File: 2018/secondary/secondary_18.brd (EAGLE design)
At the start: 160 x 173.7 mm, 35 parts, among them Q1 BUZ11BV, Q2 BUZ11BV

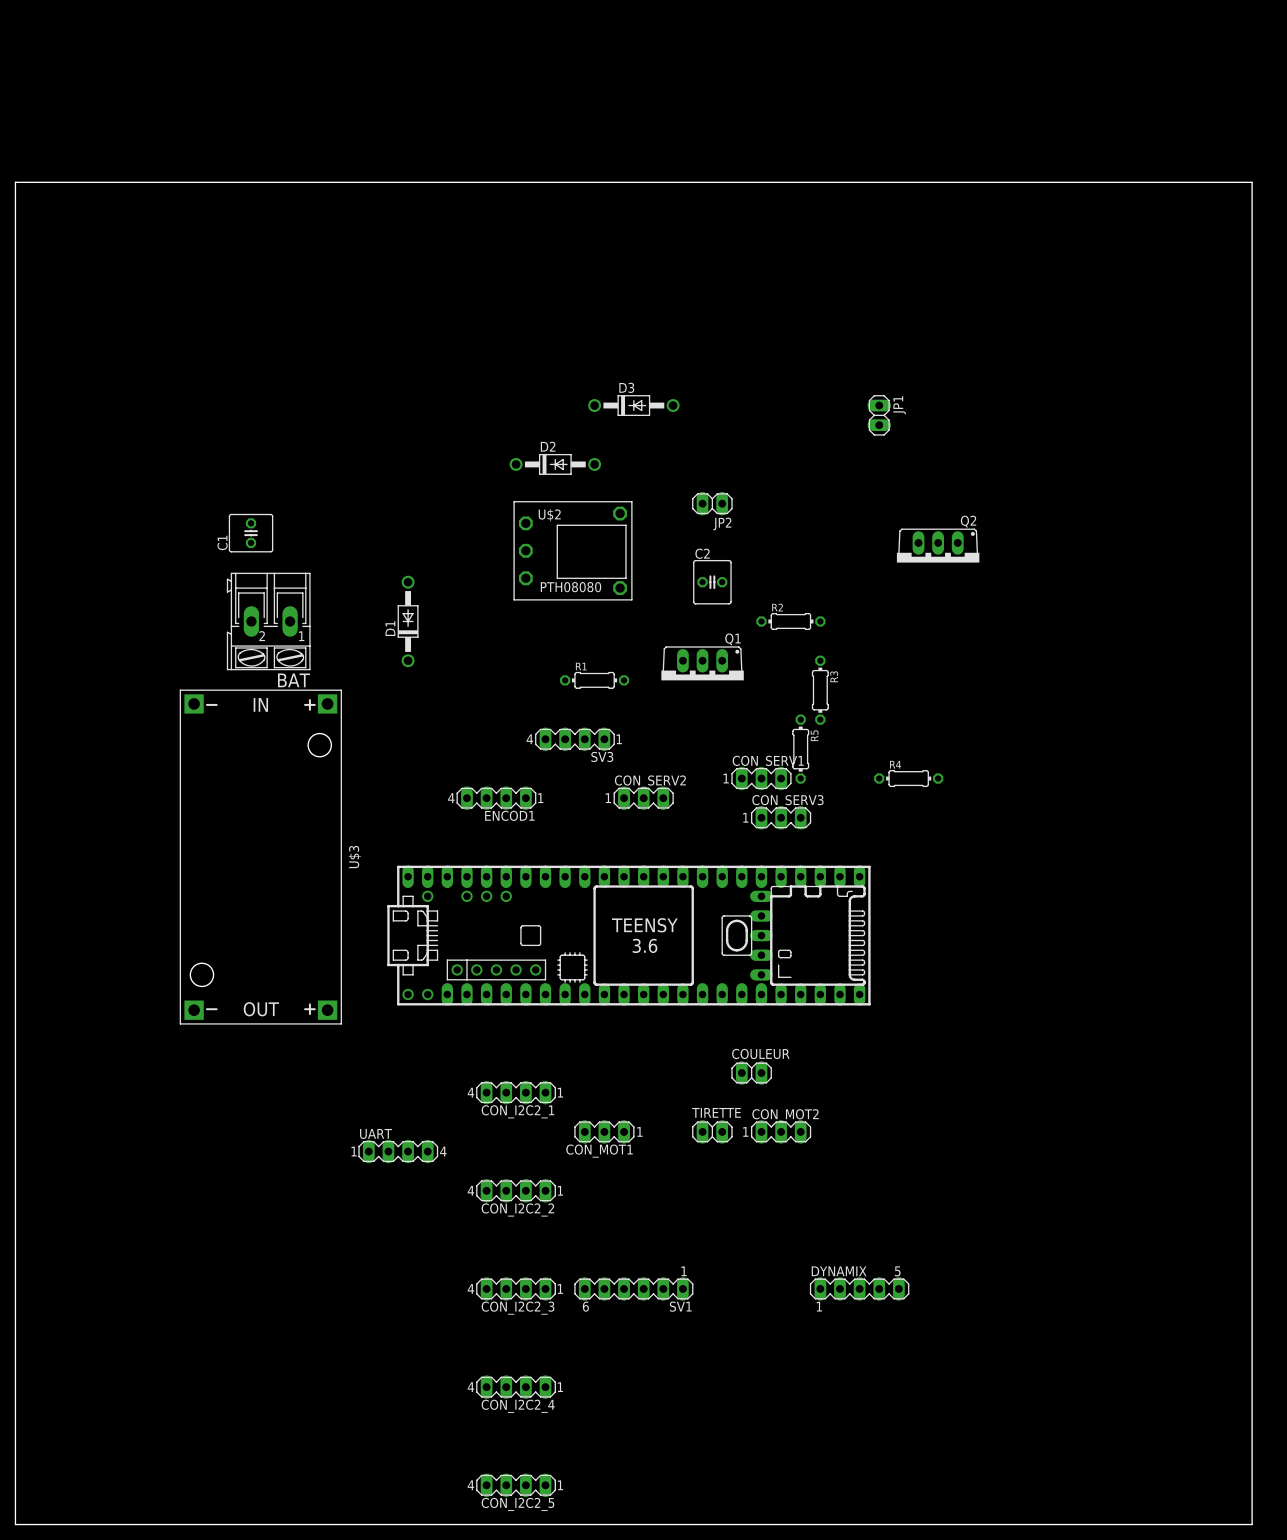
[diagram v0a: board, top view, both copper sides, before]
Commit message: [secondary 2018] Modificates the position of the elements above the x abscisse
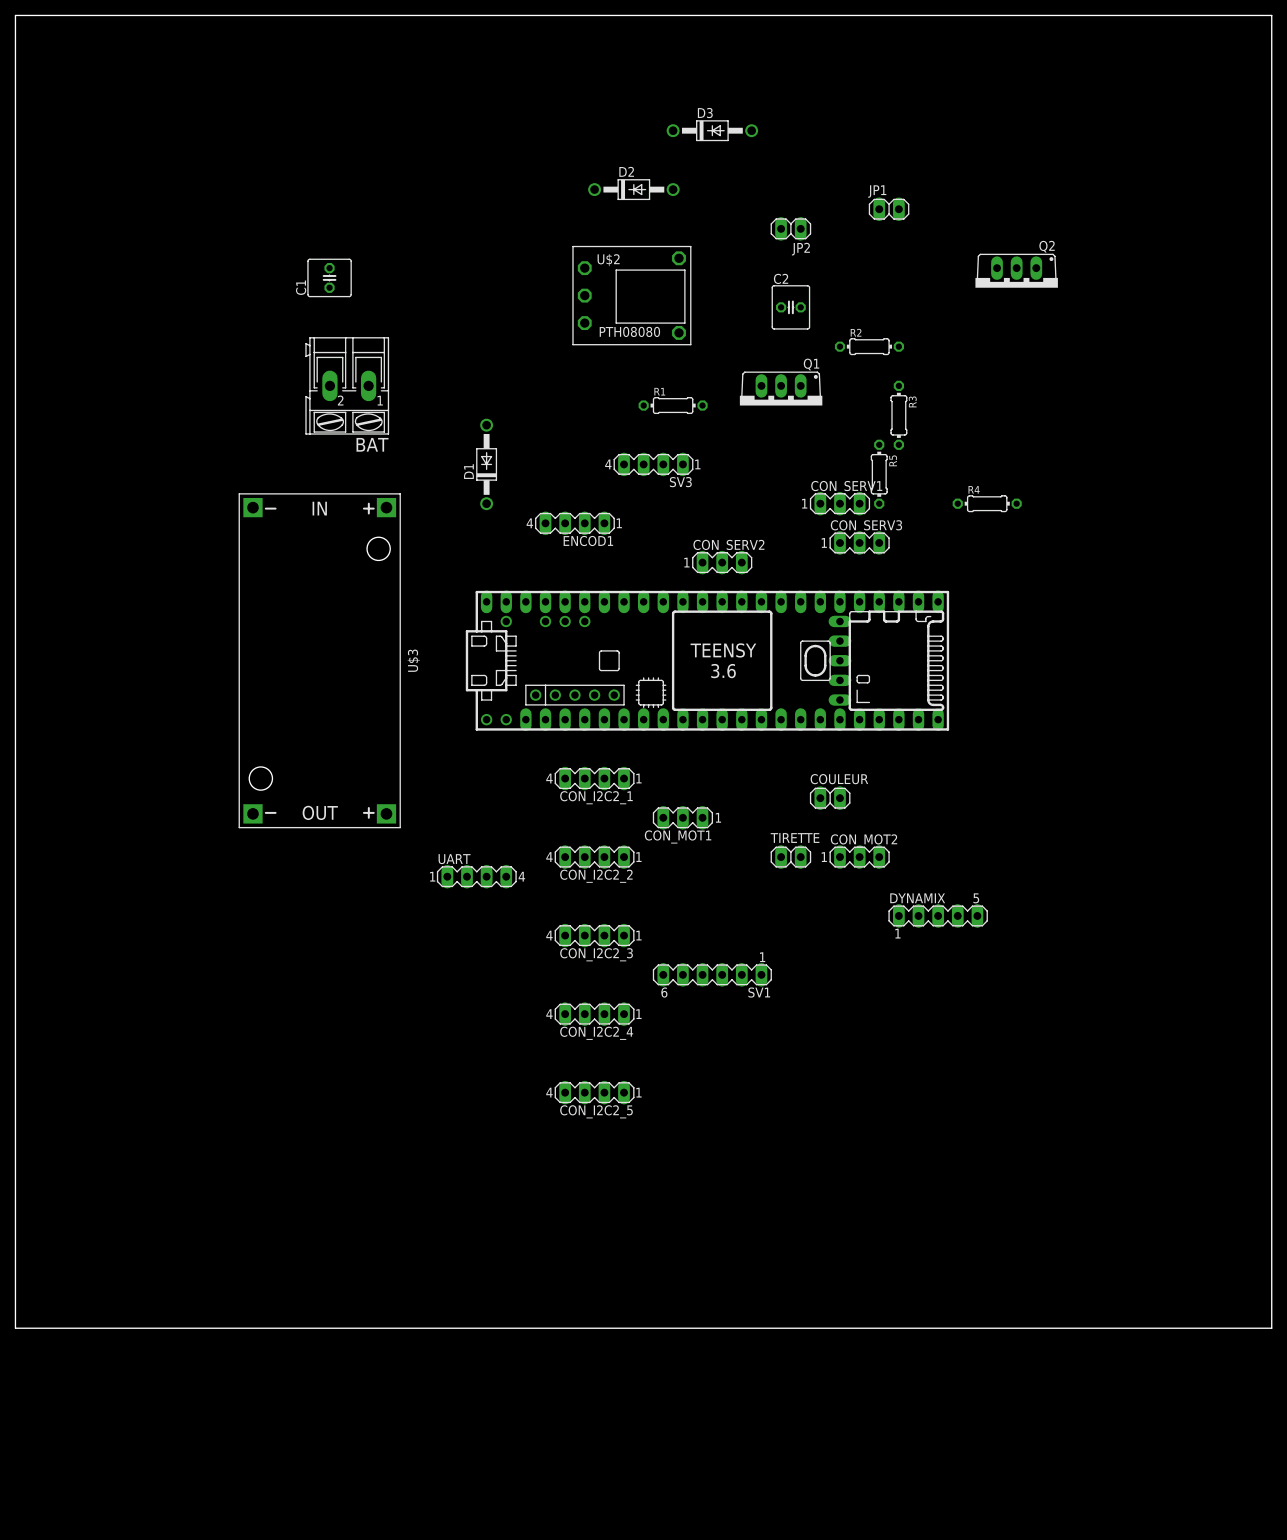
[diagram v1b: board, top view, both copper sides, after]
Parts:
- moved CON_I2C2_5 51.8 mm to (74.9, 30.5)
- moved DYNAMIX 49.3 mm to (119.4, 53.3)
- moved CON_I2C2_4 49.3 mm to (74.9, 40.6)
- moved CON_I2C2_3 46.8 mm to (74.9, 50.8)
- moved CON_I2C2_2 44.4 mm to (74.9, 61.0)
- moved CON_MOT1 41.9 mm to (86.4, 66.0)
- moved CON_I2C2_1 41.9 mm to (74.9, 71.1)
- moved SV1 41.9 mm to (90.2, 45.7)
- moved C2 37.0 mm to (100.3, 132.1)
- moved CON_MOT2 37.0 mm to (109.2, 61.0)
- moved CON_SERV1 37.0 mm to (106.7, 106.7)
- moved D3 37.0 mm to (90.2, 154.9)
- moved ENCOD1 37.0 mm to (72.4, 104.1)
- moved JP2 37.0 mm to (100.3, 142.2)
- moved Q1 37.0 mm to (99.1, 119.4)
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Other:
- board size 160 x 173.7 mm -> 162.5 x 169.8 mm

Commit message: [secondary] Adds the final board
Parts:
- removed C1, C2: (no value), rcl:C025-060X050
- removed D1: 1N4004, diode:DO41-10
- removed R1: 348, resistor:0204/7
- removed U$2: PTH08080, pth08080:PTH08080EUF
- added U1: TSR_1-2450, SamacSys_Parts:TSR-1-24120
- moved JP1 94.5 mm to (41.9, 82.5)
- moved CON_I2C2_1 94.3 mm to (7.62, 5.08)
- moved D3 90.9 mm to (40.6, 78.7)
- moved Q2 85.4 mm to (72.4, 71.1), turned to 0 degrees
- moved CON_SERV1 83.6 mm to (39.4, 57.1), turned to 90 degrees
- moved SV3 82.9 mm to (19.1, 58.4)
- moved R4 81.7 mm to (57.1, 62.2), turned to 180 degrees
- moved ENCOD1 81.3 mm to (8.89, 53.3)
- moved BAT 80.3 mm to (88.9, 55.9), turned to 90 degrees
- moved R3 79.3 mm to (68.6, 53.3)
- moved CON_SERV3 77.5 mm to (45.7, 57.1), turned to 90 degrees
- moved CON_I2C2_2 77.3 mm to (21.6, 5.08)
- moved U$3 77.0 mm to (86.4, 25.4)
- moved R2 76.7 mm to (73.7, 59.7), turned to 180 degrees
- moved R5 76.4 mm to (59.7, 54.6)
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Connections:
- removed net N$1: R1.2, U$2.4
- net 12V: now also U1.1; no longer C2.2, D1.C, U$2.1
- net 5V_SIG: now also U1.3; no longer C1.1, D1.A, U$2.3
- net GND: now also U1.2; no longer C1.2, C2.1, R1.1, U$2.2
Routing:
- net 5V_SIG: track 0.00 -> 288.3 mm
- net 12V: track 0.00 -> 151.5 mm
- net 5V_PUI: track 0.00 -> 98.0 mm
- net N$23: track 0.00 -> 67.2 mm
- net N$21: track 0.00 -> 54.8 mm
- net GND: track 0.00 -> 27.5 mm, vias 0 -> 8
- net N$24: track 0.00 -> 23.5 mm
- net N$8: track 0.00 -> 23.0 mm
- net N$20: track 0.00 -> 22.2 mm
- net N$13: track 0.00 -> 21.1 mm
- net N$18: track 0.00 -> 20.9 mm
- net N$9: track 0.00 -> 20.3 mm
- net N$19: track 0.00 -> 19.9 mm
- net N$4: track 0.00 -> 19.3 mm
- net N$15: track 0.00 -> 19.0 mm
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- added copper zone on layer 16, net GND
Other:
- board size 162.5 x 169.8 mm -> 100.4 x 86.2 mm
- board text added: "Adrien@ENAC 2018 Secondaire"
